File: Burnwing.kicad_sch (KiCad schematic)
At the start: 39 parts, among them J1 USB Type C, J2 Conn_01x06_MountingPin, J3 Conn_01x02_Pin, Q2 AONR21307, U1 HUSB238, U2 BTS7030-2EPA

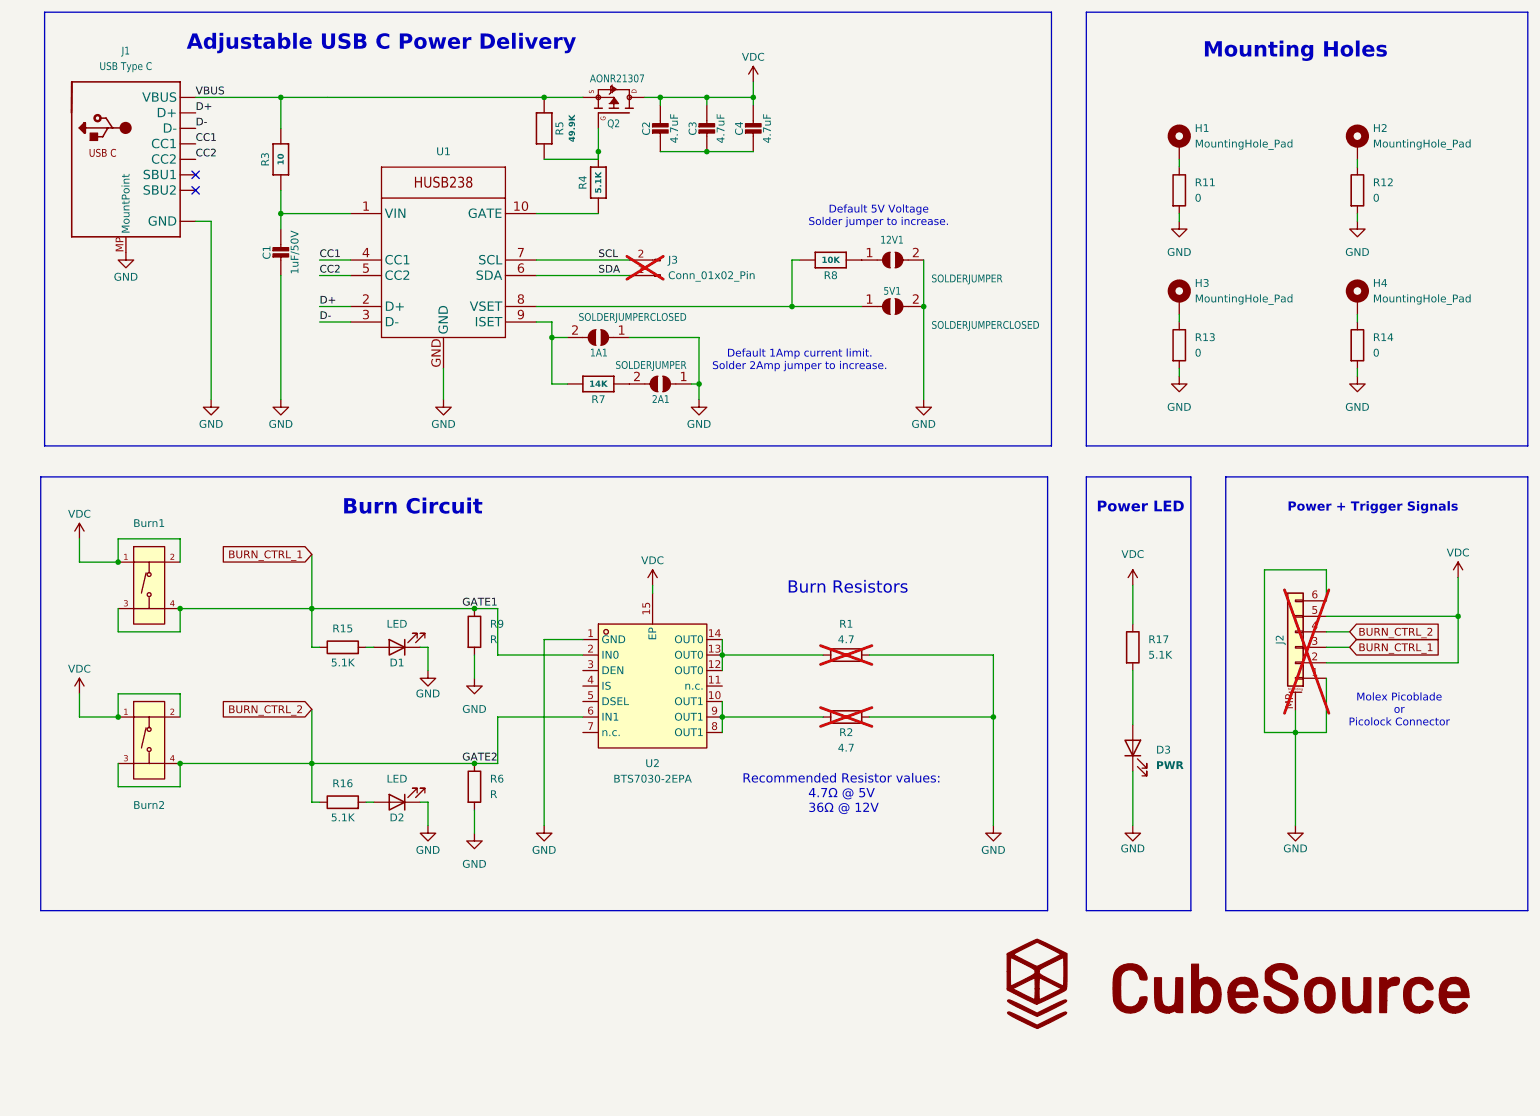
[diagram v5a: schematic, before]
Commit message: Separated Version
-Added dipswitch for Vset and Iset
-Added tentative microcontroller and jumper pins
-Separated flight and not flight modes
-Removed SCL/SDA
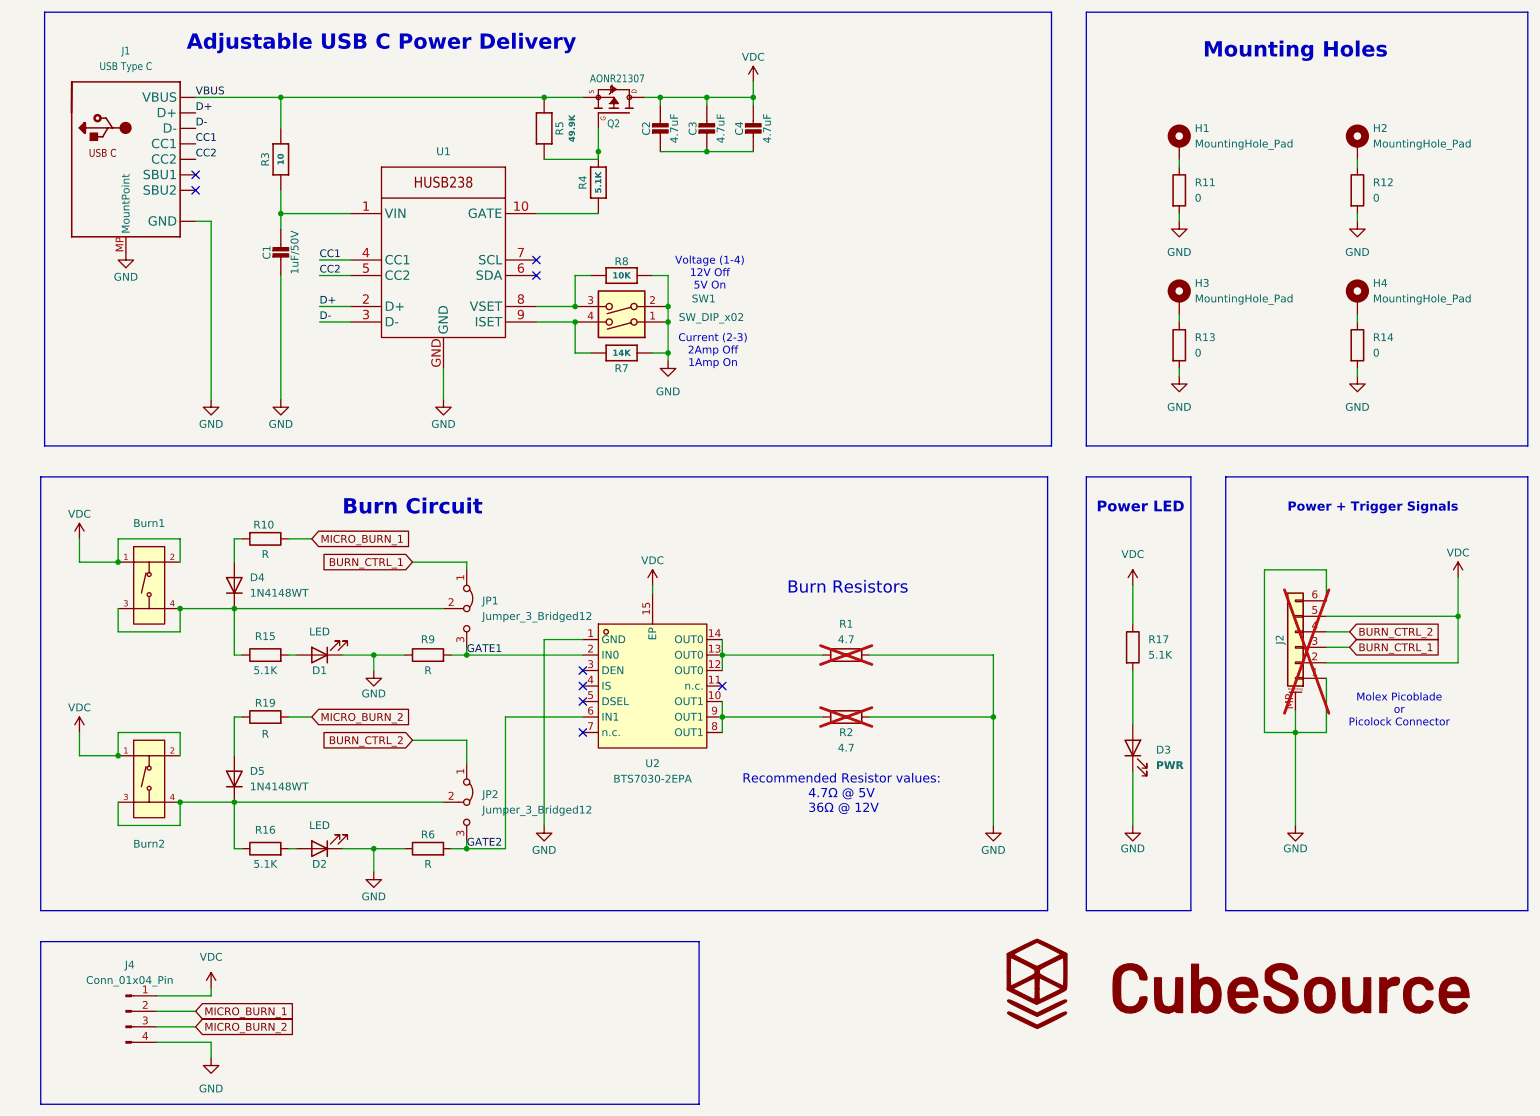
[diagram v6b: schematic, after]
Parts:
- removed 12V1, 2A1: SOLDERJUMPER, Library:SOLDERJUMPER_ARROW_NOPASTE, symbol Library:microbuilder_SOLDERJUMPER
- removed 1A1, 5V1: SOLDERJUMPERCLOSED, Library:SOLDERJUMPER_CLOSEDWIRE, symbol Library:microbuilder_SOLDERJUMPERCLOSED
- removed J3: Conn_01x02_Pin, Library:PinHeader_1x02_P1.00mm_Vertical, symbol Library:Conn_01x02_Pin
- added D4, D5: 1N4148WT, Diode_SMD:D_SOD-523, symbol Diode:1N4148WT
- added J4: Conn_01x04_Pin, Connector_PinSocket_1.00mm:PinSocket_1x04_P1.00mm_Vertical, symbol Connector:Conn_01x04_Pin
- added JP1, JP2: Jumper_3_Bridged12, Connector_PinSocket_1.00mm:PinSocket_1x03_P1.00mm_Vertical, symbol Jumper:Jumper_3_Bridged12
- added R10, R19: R, Library:R_0603_1608Metric_Pad0.98x0.95mm_HandSolder, symbol Device:R
- added SW1: SW_DIP_x02, Library:2_Dipswitch, symbol Switch:SW_DIP_x02
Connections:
- net BURN_CTRL_1: now also JP1.1 (A); no longer Burn1.3 (C), Burn1.4 (D), R15.1, R9.1, U2.2 (IN0)
- net BURN_CTRL_2: now also JP2.1 (A); no longer Burn2.3 (C), Burn2.4 (D), R16.1, R6.1, U2.6 (IN1)
- net GND: now also R6.1, R7.1, R8.1, R9.1, J4.4 (Pin_4), SW1.1, SW1.2; no longer R6.2, R9.2
- net VDC: now also J4.1 (Pin_1)
- net at R7.2, U1.9 (ISET): now also SW1.4
- net at R8.2, U1.8 (VSET): now also SW1.3
- net SCL: no longer names the net of U1.7 (SCL)
- net SDA: no longer names the net of U1.6 (SDA)
- new net: Burn1.3 (C), Burn1.4 (D), D4.1 (K), JP1.2 (C), R15.1
- new net: Burn2.3 (C), Burn2.4 (D), D5.1 (K), JP2.2 (C), R16.1
- new net: D5.2 (A), R19.1
- new net: D4.2 (A), R10.2
- new net GATE1: JP1.3 (B), R9.2, U2.2 (IN0)
- new net GATE2: JP2.3 (B), R6.2, U2.6 (IN1)
- new net MICRO_BURN_1: J4.2 (Pin_2), R10.1
- new net MICRO_BURN_2: J4.3 (Pin_3), R19.2
- no-connect marks 2 -> 9
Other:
- note added: "Current (2-3) 2Amp Off 1Amp On"
- note added: "Voltage (1-4) 12V Off 5V On"
- note removed: "Default 1Amp current limit. Solder 2Amp jumper to increase."
- note removed: "Default 5V Voltage Solder jumper to increase."
- moved on the sheet: Burn2, D1, D2, R15, R16, R6, R7, R8, R9

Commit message: Schematic Update
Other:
- note added: "Microcontroller Connections"
- moved on the sheet: J4
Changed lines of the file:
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@@
 	(rectangle
 		(start 17.78 172.72)
-		(end 125.73 199.39)
+		(end 74.93 199.39)
 		(stroke
 			(width 0)
@@
 		)
 	)
+	(text "Microcontroller Connections"
+		(exclude_from_sim no)
+		(at 46.228 176.53 0)
+		(effects
+			(font
+				(size 2.5 2.5)
+				(thickness 0.5)
+				(bold yes)
+			)
+		)
+	)
 	(text "Power LED"
 		(exclude_from_sim no)
@@
 	(wire
 		(pts
-			(xy 36.83 184.15) (xy 43.18 184.15)
+			(xy 39.37 187.96) (xy 45.72 187.96)
 		)
 		(stroke
@@
 	(wire
 		(pts
-			(xy 36.83 186.69) (xy 43.18 186.69)
+			(xy 39.37 190.5) (xy 45.72 190.5)
 		)
 		(stroke
@@
 	(wire
 		(pts
-			(xy 36.83 181.61) (xy 45.72 181.61)
+			(xy 39.37 185.42) (xy 48.26 185.42)
 		)
 		(stroke
@@
 	(wire
 		(pts
-			(xy 45.72 189.23) (xy 45.72 191.77)
+			(xy 48.26 193.04) (xy 48.26 195.58)
 		)
 		(stroke
@@
 	(wire
 		(pts
-			(xy 36.83 189.23) (xy 45.72 189.23)
+			(xy 39.37 193.04) (xy 48.26 193.04)
 		)
 		(stroke
@@
 	(wire
 		(pts
-			(xy 45.72 181.61) (xy 45.72 180.34)
+			(xy 48.26 185.42) (xy 48.26 184.15)
 		)
 		(stroke
@@
 	(global_label "MICRO_BURN_2"
 		(shape input)
-		(at 43.18 186.69 0)
+		(at 45.72 190.5 0)
 		(fields_autoplaced yes)
 		(effects
@@
 		)
 		(property "Intersheetrefs" "${INTERSHEET_REFS}"
-			(at 60.4376 186.69 0)
+			(at 62.9776 190.5 0)
 			(effects
 				(font
@@
 	(global_label "MICRO_BURN_1"
 		(shape input)
-		(at 43.18 184.15 0)
+		(at 45.72 187.96 0)
 		(fields_autoplaced yes)
 		(effects
@@
 		)
 		(property "Intersheetrefs" "${INTERSHEET_REFS}"
-			(at 60.4376 184.15 0)
+			(at 62.9776 187.96 0)
 			(effects
 				(font
@@
 	(symbol
 		(lib_id "power:GND")
-		(at 45.72 191.77 0)
+		(at 48.26 195.58 0)
 		(unit 1)
 		(exclude_from_sim no)
@@
 		(on_board yes)
 		(dnp no)
-		(fields_autoplaced yes)
 		(property "Reference" "#PWR026"
-			(at 45.72 198.12 0)
+			(at 48.26 201.93 0)
 			(effects
 				(font
@@
 		)
 		(property "Value" "GND"
-			(at 45.72 196.85 0)
+			(at 52.324 197.358 0)
 			(effects
 				(font
@@
 		)
 		(property "Footprint" ""
-			(at 45.72 191.77 0)
+			(at 48.26 195.58 0)
 			(effects
 				(font
@@
 		)
 		(property "Datasheet" ""
-			(at 45.72 191.77 0)
+			(at 48.26 195.58 0)
 			(effects
 				(font
@@
 		)
 		(property "Description" "Power symbol creates a global label with name \"GND\" , ground"
-			(at 45.72 191.77 0)
+			(at 48.26 195.58 0)
 			(effects
 				(font
@@
 	(symbol
 		(lib_id "Connector:Conn_01x04_Pin")
-		(at 31.75 184.15 0)
+		(at 34.29 187.96 0)
 		(unit 1)
 		(exclude_from_sim no)
@@
 		(fields_autoplaced yes)
 		(property "Reference" "J4"
-			(at 32.385 176.53 0)
+			(at 34.925 180.34 0)
 			(effects
 				(font
@@
 		)
 		(property "Value" "Conn_01x04_Pin"
-			(at 32.385 179.07 0)
+			(at 34.925 182.88 0)
 			(effects
 				(font
@@
 		)
 		(property "Footprint" "Connector_PinSocket_1.00mm:PinSocket_1x04_P1.00mm_Vertical"
-			(at 31.75 184.15 0)
+			(at 34.29 187.96 0)
 			(effects
 				(font
@@
 		)
 		(property "Datasheet" "~"
-			(at 31.75 184.15 0)
+			(at 34.29 187.96 0)
 			(effects
 				(font
@@
 		)
 		(property "Description" "Generic connector, single row, 01x04, script generated"
-			(at 31.75 184.15 0)
+			(at 34.29 187.96 0)
 			(effects
 				(font
@@
 	(symbol
 		(lib_id "power:VDC")
-		(at 45.72 180.34 0)
+		(at 48.26 184.15 0)
 		(unit 1)
 		(exclude_from_sim no)
@@
 		(on_board yes)
 		(dnp no)
-		(fields_autoplaced yes)
 		(property "Reference" "#PWR025"
-			(at 45.72 184.15 0)
+			(at 48.26 187.96 0)
 			(effects
 				(font
@@
 		)
 		(property "Value" "VDC"
-			(at 45.72 175.26 0)
+			(at 48.006 180.34 0)
 			(effects
 				(font
@@
 		)
 		(property "Footprint" ""
-			(at 45.72 180.34 0)
+			(at 48.26 184.15 0)
 			(effects
 				(font
@@
 		)
 		(property "Datasheet" ""
-			(at 45.72 180.34 0)
+			(at 48.26 184.15 0)
 			(effects
 				(font
@@
 		)
 		(property "Description" "Power symbol creates a global label with name \"VDC\""
-			(at 45.72 180.34 0)
+			(at 48.26 184.15 0)
 			(effects
 				(font

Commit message: Fixed VDC traces
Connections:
- net GND: now also C2.2, C3.2, C4.2
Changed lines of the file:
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@@
+	(wire
+		(pts
+			(xy 127 46.99) (xy 127 43.18)
+		)
+		(stroke
+			(width 0)
+			(type default)
+		)
+	)
 	(wire
 		(pts
@@
 					(unit 1)
 				)
+			)
+		)
+	)
+	(symbol
+		(lib_id "power:GND")
+		(at 127 46.99 0)
+		(unit 1)
+		(exclude_from_sim no)
+		(in_bom yes)
+		(on_board yes)
+		(dnp no)
+		(fields_autoplaced yes)
+		(property "Reference" "#PWR024"
+			(at 127 53.34 0)
+			(effects
+				(font
+					(size 1.27 1.27)
+				)
+				(hide yes)
+			)
+		)
+		(property "Value" "GND"
+			(at 127 52.07 0)
+			(effects
+				(font
+					(size 1.27 1.27)
+				)
+			)
+		)
+		(property "Footprint" ""
+			(at 127 46.99 0)
+			(effects
+				(font
+					(size 1.27 1.27)
+				)
+				(hide yes)
+			)
+		)
+		(property "Datasheet" ""
+			(at 127 46.99 0)
+			(effects
+				(font
+					(size 1.27 1.27)
+				)
+				(hide yes)
+			)
+		)
+		(property "Description" "Power symbol creates a global label with name \"GND\" , ground"
+			(at 127 46.99 0)
+			(effects
+				(font
+					(size 1.27 1.27)
+				)
+				(hide yes)
+			)
+		)
+		(pin "1"
+		)
+		(instances
+			(project "Burnwing"
+				(path "/668c3a07-3236-4b27-b3a6-03c249258f7f"
+					(reference "#PWR024")
+					(unit 1)
+				)
